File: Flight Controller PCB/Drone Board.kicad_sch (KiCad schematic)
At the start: 0 parts

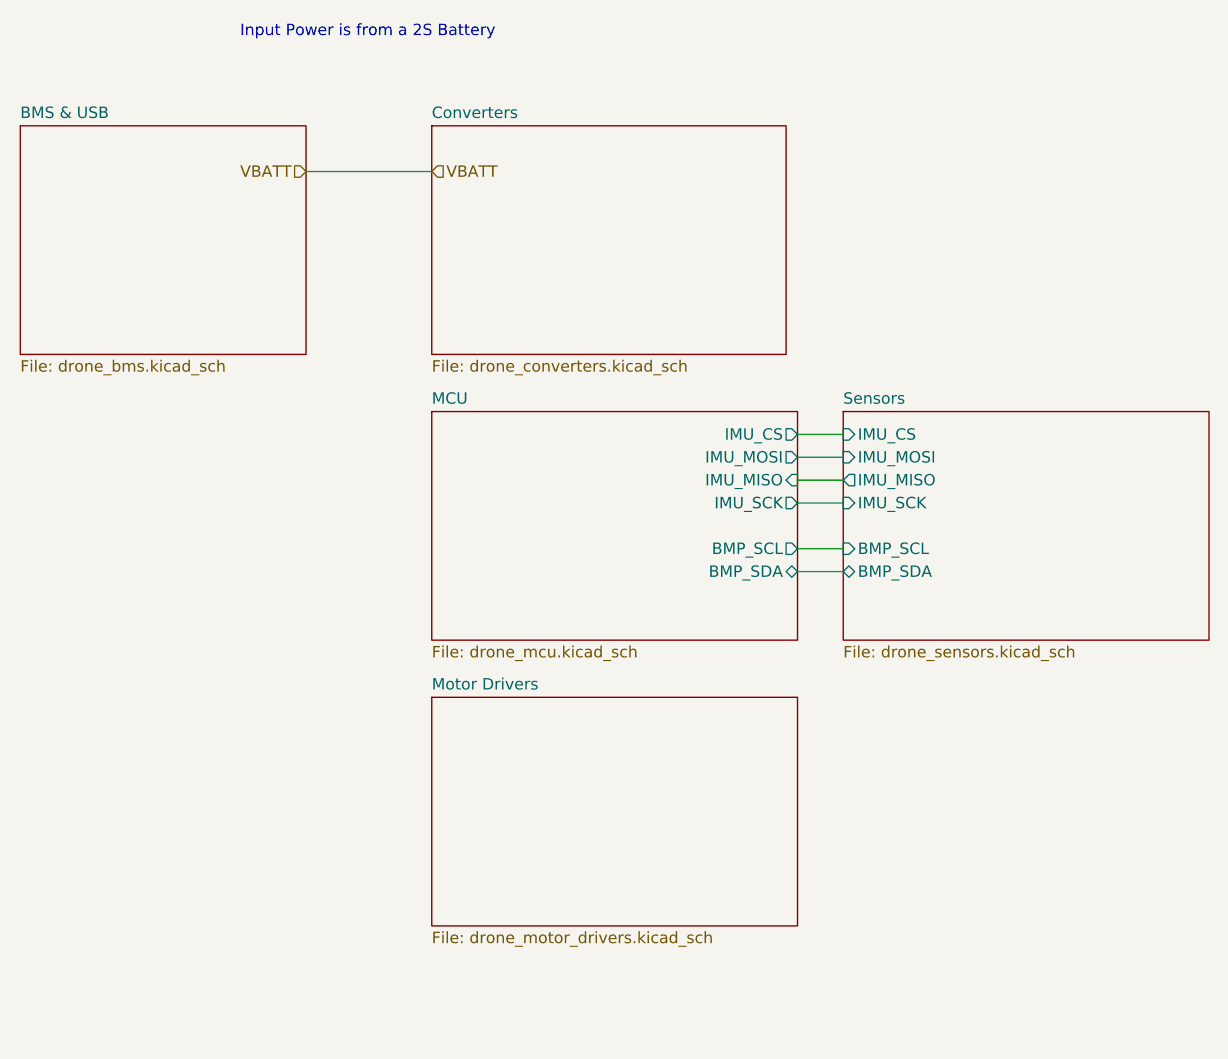
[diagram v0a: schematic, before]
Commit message: Some changes. TODO: Add power and control for RunCam2. Add battery voltage monitoring
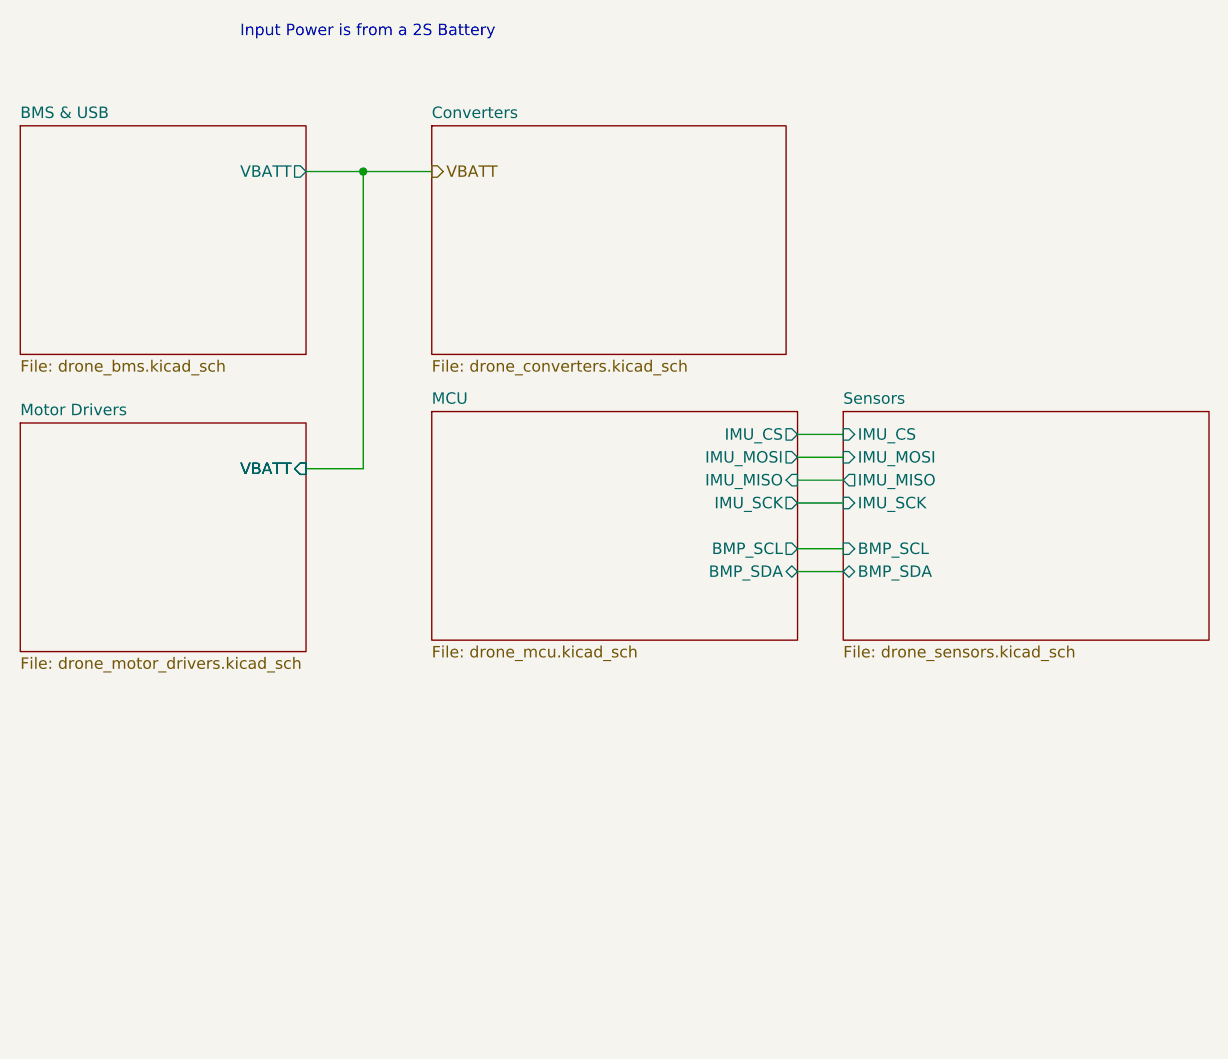
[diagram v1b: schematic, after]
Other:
- sheet BMS & USB ports: added VBATT; removed none
- sheet Motor Drivers ports: added VBATT; removed none
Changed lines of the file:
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@@
 		)
+	)
+	(junction
+		(at 73.66 40.64)
+		(diameter 0)
+		(color 0 0 0 0)
 	)
 	(wire
@@
 	(wire
 		(pts
+			(xy 73.66 73.66) (xy 73.66 40.64)
+		)
+		(stroke
+			(width 0)
+			(type default)
+		)
+	)
+	(wire
+		(pts
 			(xy 121.92 69.85) (xy 127 69.85)
 		)
@@
 	(wire
 		(pts
-			(xy 67.31 40.64) (xy 81.28 40.64)
+			(xy 67.31 40.64) (xy 73.66 40.64)
+		)
+		(stroke
+			(width 0)
+			(type default)
+		)
+	)
+	(wire
+		(pts
+			(xy 73.66 40.64) (xy 81.28 40.64)
 		)
 		(stroke
@@
 	(wire
 		(pts
+			(xy 67.31 73.66) (xy 73.66 73.66)
+		)
+		(stroke
+			(width 0)
+			(type default)
+		)
+	)
+	(wire
+		(pts
 			(xy 121.92 74.93) (xy 127 74.93)
 		)
@@
 	)
 	(hierarchical_label "VBATT"
-		(shape input)
-		(at 67.31 40.64 180)
-		(effects
-			(font
-				(size 1.27 1.27)
-			)
-			(justify right)
-		)
-	)
-	(hierarchical_label "VBATT"
-		(shape input)
+		(shape output)
 		(at 81.28 40.64 0)
 		(effects
@@
 			)
 		)
+		(pin "VBATT" output
+			(at 67.31 40.64 0)
+			(effects
+				(font
+					(size 1.27 1.27)
+				)
+				(justify right)
+			)
+		)
 		(instances
 			(project "Drone Board"
@@
 	)
 	(sheet
-		(at 81.28 99.06)
-		(size 40.64 25.4)
+		(at 35.56 68.58)
+		(size 31.75 25.4)
 		(exclude_from_sim no)
 		(in_bom yes)
@@
 		)
 		(property "Sheetname" "Motor Drivers"
-			(at 81.28 98.3484 0)
+			(at 35.56 67.8684 0)
 			(show_name no)
 			(do_not_autoplace no)
@@
 		)
 		(property "Sheetfile" "drone_motor_drivers.kicad_sch"
-			(at 81.28 125.0446 0)
+			(at 35.56 94.5646 0)
 			(show_name no)
 			(do_not_autoplace no)
@@
 			)
 		)
+		(pin "VBATT" input
+			(at 67.31 73.66 0)
+			(effects
+				(font
+					(size 1.27 1.27)
+				)
+				(justify right)
+			)
+		)
+		(pin "VBATT" input
+			(at 67.31 73.66 0)
+			(effects
+				(font
+					(size 1.27 1.27)
+				)
+				(justify right)
+			)
+		)

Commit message: Updated gitignore
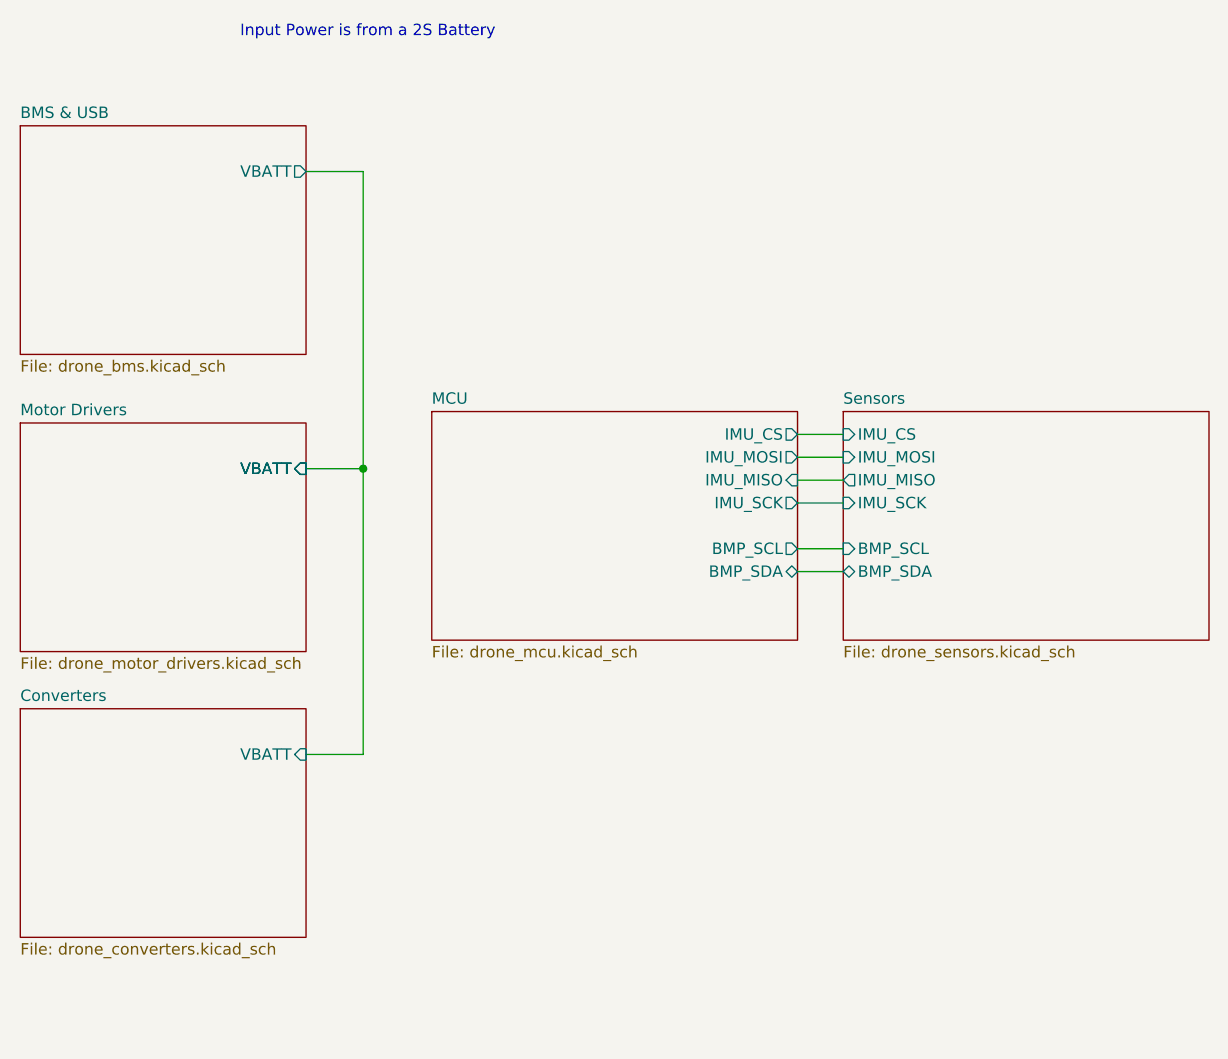
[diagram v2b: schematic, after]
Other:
- sheet Converters ports: added VBATT; removed none
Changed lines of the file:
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@@
 	)
 	(junction
-		(at 73.66 40.64)
+		(at 73.66 73.66)
 		(diameter 0)
 		(color 0 0 0 0)
@@
 	(wire
 		(pts
-			(xy 73.66 40.64) (xy 81.28 40.64)
-		)
-		(stroke
-			(width 0)
-			(type default)
-		)
-	)
-	(wire
-		(pts
 			(xy 121.92 72.39) (xy 127 72.39)
 		)
@@
 	(wire
 		(pts
+			(xy 73.66 105.41) (xy 73.66 73.66)
+		)
+		(stroke
+			(width 0)
+			(type default)
+		)
+	)
+	(wire
+		(pts
 			(xy 121.92 74.93) (xy 127 74.93)
 		)
@@
 		)
 	)
-	(hierarchical_label "VBATT"
-		(shape output)
-		(at 81.28 40.64 0)
-		(effects
-			(font
-				(size 1.27 1.27)
-			)
-			(justify left)
+	(wire
+		(pts
+			(xy 67.31 105.41) (xy 73.66 105.41)
+		)
+		(stroke
+			(width 0)
+			(type default)
 		)
 	)
@@
 	)
 	(sheet
-		(at 81.28 35.56)
-		(size 39.37 25.4)
+		(at 35.56 100.33)
+		(size 31.75 25.4)
 		(exclude_from_sim no)
 		(in_bom yes)
@@
 		)
 		(property "Sheetname" "Converters"
-			(at 81.28 34.8484 0)
+			(at 35.56 99.6184 0)
 			(show_name no)
 			(do_not_autoplace no)
@@
 		)
 		(property "Sheetfile" "drone_converters.kicad_sch"
-			(at 81.28 61.5446 0)
+			(at 35.56 126.3146 0)
 			(show_name no)
 			(do_not_autoplace no)
@@
 			)
 		)
+		(pin "VBATT" input
+			(at 67.31 105.41 0)
+			(effects
+				(font
+					(size 1.27 1.27)
+				)
+				(justify right)
+			)
+		)

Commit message: Finished converters, combined converter & sensor sheets. Updated I2C & CS pullups. TODO: Add motor control pins to MCU & control pins for camera
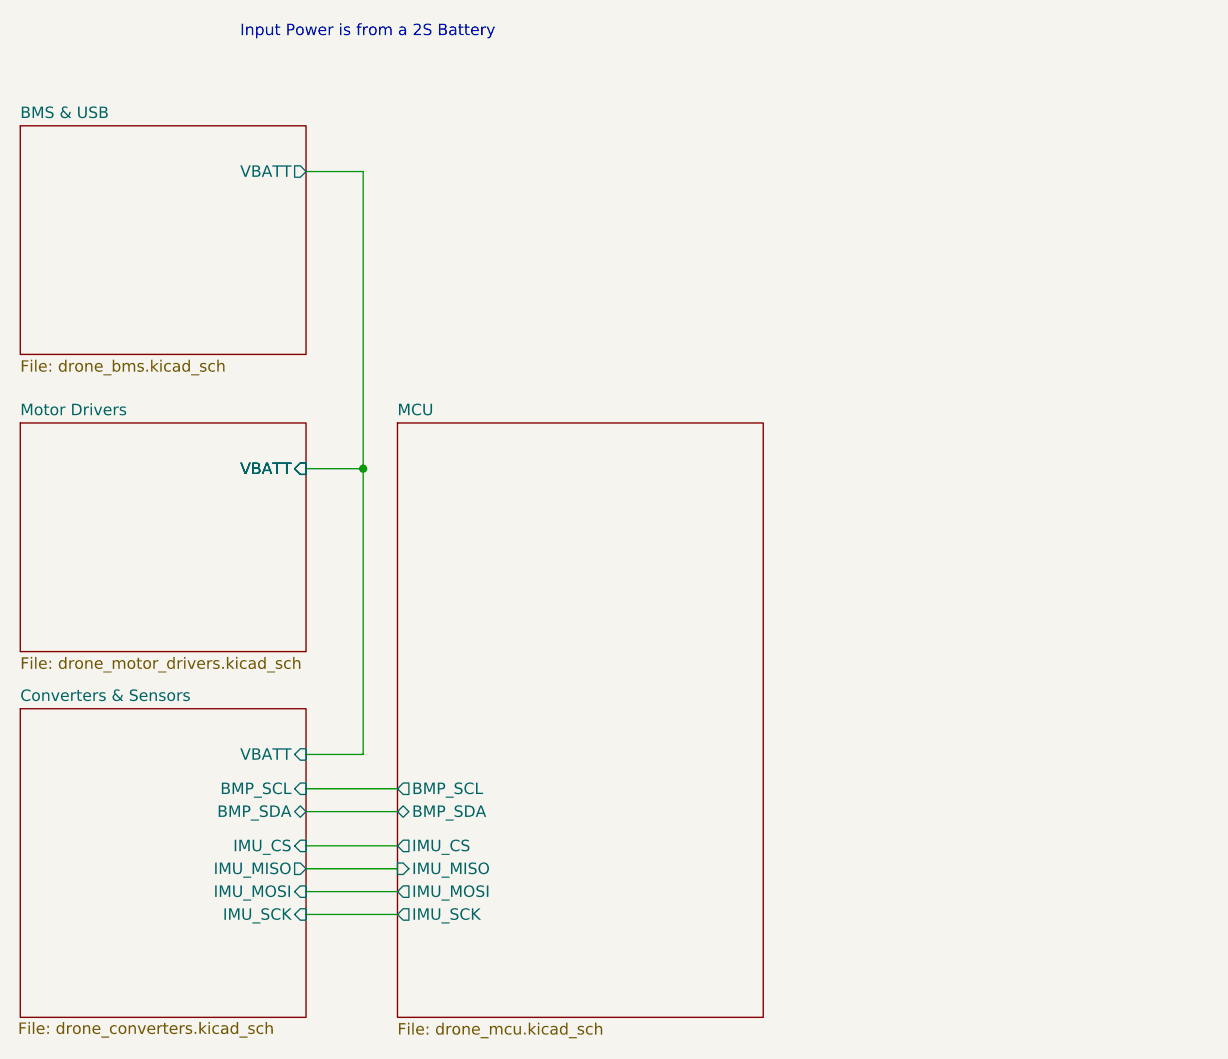
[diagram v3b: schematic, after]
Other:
- sheet Converters renamed Converters & Sensors
- removed sheet Sensors
- sheet Converters & Sensors ports: added BMP_SCL, BMP_SDA, IMU_CS, IMU_MISO, IMU_MOSI, IMU_SCK; removed none
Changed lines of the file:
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@@
 	(wire
 		(pts
-			(xy 121.92 77.47) (xy 127 77.47)
+			(xy 67.31 123.19) (xy 77.47 123.19)
 		)
 		(stroke
@@
 	(wire
 		(pts
-			(xy 121.92 69.85) (xy 127 69.85)
-		)
-		(stroke
-			(width 0)
-			(type default)
-		)
-	)
-	(wire
-		(pts
-			(xy 121.92 85.09) (xy 127 85.09)
+			(xy 67.31 111.76) (xy 77.47 111.76)
+		)
+		(stroke
+			(width 0)
+			(type default)
+		)
+	)
+	(wire
+		(pts
+			(xy 67.31 120.65) (xy 77.47 120.65)
+		)
+		(stroke
+			(width 0)
+			(type default)
+		)
+	)
+	(wire
+		(pts
+			(xy 67.31 115.57) (xy 77.47 115.57)
 		)
 		(stroke
@@
 	(wire
 		(pts
-			(xy 121.92 72.39) (xy 127 72.39)
-		)
-		(stroke
-			(width 0)
-			(type default)
-		)
-	)
-	(wire
-		(pts
-			(xy 121.92 82.55) (xy 127 82.55)
+			(xy 67.31 109.22) (xy 77.47 109.22)
+		)
+		(stroke
+			(width 0)
+			(type default)
+		)
+	)
+	(wire
+		(pts
+			(xy 67.31 118.11) (xy 77.47 118.11)
 		)
 		(stroke
@@
 		(pts
 			(xy 73.66 105.41) (xy 73.66 73.66)
-		)
-		(stroke
-			(width 0)
-			(type default)
-		)
-	)
-	(wire
-		(pts
-			(xy 121.92 74.93) (xy 127 74.93)
 		)
 		(stroke
@@
 	)
 	(sheet
-		(at 127 67.31)
-		(size 40.64 25.4)
+		(at 77.47 68.58)
+		(size 40.64 66.04)
 		(exclude_from_sim no)
 		(in_bom yes)
@@
 			(color 0 0 0 0)
 		)
-		(property "Sheetname" "Sensors"
-			(at 127 66.5984 0)
+		(property "Sheetname" "MCU"
+			(at 77.47 67.8684 0)
 			(show_name no)
 			(do_not_autoplace no)
@@
 			)
 		)
-		(property "Sheetfile" "drone_sensors.kicad_sch"
-			(at 127 93.2946 0)
+		(property "Sheetfile" "drone_mcu.kicad_sch"
+			(at 77.47 135.2046 0)
 			(show_name no)
 			(do_not_autoplace no)
@@
 			)
 		)
+		(pin "BMP_SCL" output
+			(at 77.47 109.22 180)
+			(effects
+				(font
+					(size 1.27 1.27)
+				)
+				(justify left)
+			)
+		)
 		(pin "BMP_SDA" bidirectional
-			(at 127 85.09 180)
-			(effects
-				(font
-					(size 1.27 1.27)
-				)
-				(justify left)
-			)
-		)
-		(pin "BMP_SCL" input
-			(at 127 82.55 180)
-			(effects
-				(font
-					(size 1.27 1.27)
-				)
-				(justify left)
-			)
-		)
-		(pin "IMU_CS" input
-			(at 127 69.85 180)
-			(effects
-				(font
-					(size 1.27 1.27)
-				)
-				(justify left)
-			)
-		)
-		(pin "IMU_MISO" output
-			(at 127 74.93 180)
-			(effects
-				(font
-					(size 1.27 1.27)
-				)
-				(justify left)
-			)
-		)
-		(pin "IMU_SCK" input
-			(at 127 77.47 180)
-			(effects
-				(font
-					(size 1.27 1.27)
-				)
-				(justify left)
-			)
-		)
-		(pin "IMU_MOSI" input
-			(at 127 72.39 180)
+			(at 77.47 111.76 180)
+			(effects
+				(font
+					(size 1.27 1.27)
+				)
+				(justify left)
+			)
+		)
+		(pin "IMU_SCK" output
+			(at 77.47 123.19 180)
+			(effects
+				(font
+					(size 1.27 1.27)
+				)
+				(justify left)
+			)
+		)
+		(pin "IMU_CS" output
+			(at 77.47 115.57 180)
+			(effects
+				(font
+					(size 1.27 1.27)
+				)
+				(justify left)
+			)
+		)
+		(pin "IMU_MOSI" output
+			(at 77.47 120.65 180)
+			(effects
+				(font
+					(size 1.27 1.27)
+				)
+				(justify left)
+			)
+		)
+		(pin "IMU_MISO" input
+			(at 77.47 118.11 180)
 			(effects
 				(font
@@
 			(project "Drone Board"
 				(path "/11d338fc-6b4d-4a31-a103-caeefef24b64"
-					(page "5")
+					(page "4")
 				)
 			)
@@
 	)
 	(sheet
-		(at 81.28 67.31)
-		(size 40.64 25.4)
+		(at 35.56 100.33)
+		(size 31.75 34.29)
 		(exclude_from_sim no)
 		(in_bom yes)
 		(on_board yes)
 		(dnp no)
-		(fields_autoplaced yes)
 		(stroke
 			(width 0.1524)
@@
 			(color 0 0 0 0)
 		)
-		(property "Sheetname" "MCU"
-			(at 81.28 66.5984 0)
+		(property "Sheetname" "Converters & Sensors"
+			(at 35.56 99.6184 0)
 			(show_name no)
 			(do_not_autoplace no)
@@
 			)
 		)
-		(property "Sheetfile" "drone_mcu.kicad_sch"
-			(at 81.28 93.2946 0)
-			(show_name no)
-			(do_not_autoplace no)
-			(effects
-				(font
-					(size 1.27 1.27)
-				)
-				(justify left top)
-			)
-		)
-		(pin "BMP_SCL" output
-			(at 121.92 82.55 0)
-			(effects
-				(font
-					(size 1.27 1.27)
-				)
-				(justify right)
-			)
-		)
-		(pin "BMP_SDA" bidirectional
-			(at 121.92 85.09 0)
-			(effects
-				(font
-					(size 1.27 1.27)
-				)
-				(justify right)
-			)
-		)
-		(pin "IMU_SCK" output
-			(at 121.92 77.47 0)
-			(effects
-				(font
-					(size 1.27 1.27)
-				)
-				(justify right)
-			)
-		)
-		(pin "IMU_CS" output
-			(at 121.92 69.85 0)
-			(effects
-				(font
-					(size 1.27 1.27)
-				)
-				(justify right)
-			)
-		)
-		(pin "IMU_MOSI" output
-			(at 121.92 72.39 0)
-			(effects
-				(font
-					(size 1.27 1.27)
-				)
-				(justify right)
-			)
-		)
-		(pin "IMU_MISO" input
-			(at 121.92 74.93 0)
-			(effects
-				(font
-					(size 1.27 1.27)
-				)
-				(justify right)
-			)
-		)
-		(instances
-			(project "Drone Board"
-				(path "/11d338fc-6b4d-4a31-a103-caeefef24b64"
-					(page "4")
-				)
-			)
-		)
-	)
-	(sheet
-		(at 35.56 100.33)
-		(size 31.75 25.4)
-		(exclude_from_sim no)
-		(in_bom yes)
-		(on_board yes)
-		(dnp no)
-		(fields_autoplaced yes)
-		(stroke
-			(width 0.1524)
-			(type solid)
-		)
-		(fill
-			(color 0 0 0 0)
-		)
-		(property "Sheetname" "Converters"
-			(at 35.56 99.6184 0)
-			(show_name no)
-			(do_not_autoplace no)
-			(effects
-				(font
-					(size 1.27 1.27)
-				)
-				(justify left bottom)
-			)
-		)
 		(property "Sheetfile" "drone_converters.kicad_sch"
-			(at 35.56 126.3146 0)
+			(at 35.306 135.128 0)
 			(show_name no)
 			(do_not_autoplace no)
@@
 			(effects
 				(font
+					(size 1.27 1.27)
+				)
+				(justify right)
+			)
+		)
+		(pin "IMU_SCK" input
+			(at 67.31 123.19 0)
+			(effects
+				(font
+					(size 1.27 1.27)
+				)
+				(justify right)
+			)
+		)
+		(pin "IMU_MISO" output
+			(at 67.31 118.11 0)
+			(effects
+				(font
+					(size 1.27 1.27)
+				)
+				(justify right)
+			)
+		)
+		(pin "IMU_MOSI" input
+			(at 67.31 120.65 0)
+			(effects
+				(font
+					(size 1.27 1.27)
+				)
+				(justify right)
+			)
+		)
+		(pin "IMU_CS" input
+			(at 67.31 115.57 0)
+			(effects
+				(font
+					(size 1.27 1.27)
+				)
+				(justify right)
+			)
+		)
+		(pin "BMP_SDA" bidirectional
+			(at 67.31 111.76 0)
+			(effects
+				(font
+					(size 1.27 1.27)
+				)
+				(justify right)
+			)
+		)
+		(pin "BMP_SCL" input
+			(at 67.31 109.22 0)
+			(effects
+				(font
